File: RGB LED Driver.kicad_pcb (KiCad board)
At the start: 2 copper layers, 97.1 x 75.7 mm, 106 parts, among them J1 USB_C_Receptacle_USB2.0, J2 Conn_01x06_Pin, Q1 AO3400A, Q2 AO3400A, Q3 AO3400A, Q4 AO3400A, SW1 BOOT, U1 TPS61170DRVR, U10 LM358, U2 AP2112K-3.3TRG1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

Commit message: laid out stuff
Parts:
- removed kibuzzard-6592DDAB: G***, kibuzzard-6592DDAB
- added C16: 1uF, Capacitor_SMD:C_0805_2012Metric_Pad1.18x1.45mm_HandSolder, F.Cu at (90.0, 59.0)
- added C17: 1uF, Capacitor_SMD:C_0805_2012Metric_Pad1.18x1.45mm_HandSolder, F.Cu at (127.0, 83.7)
- added C18: 1uF, Capacitor_SMD:C_0805_2012Metric_Pad1.18x1.45mm_HandSolder, F.Cu at (127.0, 81.2)
- added D44: RED LED, LED_SMD:LED_0805_2012Metric_Pad1.15x1.40mm_HandSolder, F.Cu at (171.0, 86.5)
- added R28: 10K, Resistor_SMD:R_0805_2012Metric_Pad1.20x1.40mm_HandSolder, F.Cu at (109.5, 78.0)
- added R29: 300K, Resistor_SMD:R_0805_2012Metric_Pad1.20x1.40mm_HandSolder, F.Cu at (168.0, 86.5)
- added TP1: 5260 (Red), TestPoint:TestPoint_Keystone_5000-5004_Miniature, F.Cu at (143.5, 57.0)
- added TP2: 5264 (Yellow), TestPoint:TestPoint_Keystone_5000-5004_Miniature, F.Cu at (174.0, 86.0)
- added TP3: 5261 (Black), TestPoint:TestPoint_Keystone_5000-5004_Miniature, F.Cu at (143.5, 68.0)
- added TP4: 5261 (Black), TestPoint:TestPoint_Keystone_5000-5004_Miniature, F.Cu at (165.0, 86.0)
- added TP5: 5269 (Purple), TestPoint:TestPoint_Keystone_5000-5004_Miniature, F.Cu at (117.5, 56.8)
- added TP6: 5269 (Purple), TestPoint:TestPoint_Keystone_5000-5004_Miniature, F.Cu at (117.5, 60.2)
- added TP7: 5269 (Purple), TestPoint:TestPoint_Keystone_5000-5004_Miniature, F.Cu at (117.5, 63.8)
- added TP8: 5269 (Purple), TestPoint:TestPoint_Keystone_5000-5004_Miniature, F.Cu at (117.5, 67.2)
- added kibuzzard-65932266: G***, kibuzzard-65932266, F.Cu at (143.5, 54.6)
- added kibuzzard-65932378: G***, kibuzzard-65932378, F.Cu at (165.0, 88.8)
- added kibuzzard-65932378: G***, kibuzzard-65932378, F.Cu at (143.5, 70.8)
- added kibuzzard-6593238E: G***, kibuzzard-6593238E, F.Cu at (174.0, 88.8)
- added kibuzzard-659323CF: G***, kibuzzard-659323CF, F.Cu at (131.5, 88.0)
- added kibuzzard-65932434: G***, kibuzzard-65932434, F.Cu at (106.2, 86.2)
- added kibuzzard-65932443: G***, kibuzzard-65932443, F.Cu at (156.0, 81.0)
- added kibuzzard-65932491: G***, kibuzzard-65932491, F.Cu at (99.0, 86.5)
- added kibuzzard-659324E3: G***, kibuzzard-659324E3, F.Cu at (117.0, 81.8)
- added kibuzzard-65932565: G***, kibuzzard-65932565, F.Cu at (90.0, 86.8)
- added kibuzzard-659325DE: G***, kibuzzard-659325DE, F.Cu at (142.8, 130.8)
- added kibuzzard-65932806: G***, kibuzzard-65932806, F.Cu at (100.5, 130.8)
- added kibuzzard-65932B20: G***, kibuzzard-65932B20, F.Cu at (122.2, 56.8)
- added kibuzzard-65932B45: G***, kibuzzard-65932B45, F.Cu at (122.2, 67.2)
- added kibuzzard-65932B4E: G***, kibuzzard-65932B4E, F.Cu at (122.2, 63.8)
- added kibuzzard-65932B54: G***, kibuzzard-65932B54, F.Cu at (122.2, 60.2)
- added kibuzzard-65932F0E: G***, kibuzzard-65932F0E, F.Cu at (89.0, 125.0)
- added kibuzzard-65932F14: G***, kibuzzard-65932F14, F.Cu at (89.0, 115.0)
- added kibuzzard-65932F1A: G***, kibuzzard-65932F1A, F.Cu at (88.9, 105.4)
- added kibuzzard-65932F21: G***, kibuzzard-65932F21, F.Cu at (88.9, 95.2)
- added kibuzzard-6593379A: G***, kibuzzard-6593379A, F.Cu at (147.5, 84.5)
- C11: value 10uF -> 1uF
- C2: footprint rgb_led_driver_footprints:EEHZA1J100P -> Capacitor_SMD:CP_Elec_6.3x5.8
- J2: footprint Connector_PinSocket_2.54mm:PinSocket_1x06_P2.54mm_Vertical -> Connector_PinHeader_2.54mm:PinHeader_1x06_P2.54mm_Vertical
- moved R7 58.2 mm to (143.5, 60.0)
- moved D2 52.8 mm to (143.5, 63.5)
- moved NT1 30.6 mm to (169.4, 84.0)
- moved D3 19.0 mm to (90.0, 77.0)
- moved R14 17.0 mm to (90.0, 80.5), turned to 180 degrees
- moved C7 16.0 mm to (90.0, 65.0), turned to 0 degrees
- moved U5 15.4 mm to (133.6, 80.0), turned to -90 degrees
- moved J2 12.8 mm to (98.9, 83.0)
- moved C13 10.4 mm to (94.6, 105.2)
- moved C14 10.3 mm to (94.6, 115.0)
- moved C15 10.3 mm to (94.6, 124.8)
- moved C12 10.2 mm to (94.5, 95.1)
- moved R23 9.57 mm to (111.8, 127.2), turned to 0 degrees
- moved R8 9.44 mm to (111.8, 107.4), turned to 0 degrees
- moved R17 9.37 mm to (111.8, 97.3), turned to 0 degrees
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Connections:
- C10 pad 1: +3.3V -> +3V3
- C9 pad 1: +3.3V -> +3V3
- U4 pad 1: Net-(J1-D+-PadA6) -> /USB-Serial/USB_N
- U4 pad 3: Net-(J1-D--PadA7) -> /USB-Serial/USB_P
- U4 pad 4: /USB-Serial/USB_N -> Net-(J1-D+-PadA6)
- U4 pad 6: /USB-Serial/USB_P -> Net-(J1-D--PadA7)
- U5 pad 16: unconnected-(U5-VPP-Pad16) -> Net-(U5-VPP)
- U5 pad 5: +3.3V -> +3V3
- U5 pad 6: +3.3V -> +3V3
- U5 pad 7: +3.3V -> +5V
- U6 pad 27: /ESP32/LED_R -> unconnected-(U6-IO16-Pad27)
- U6 pad 28: /ESP32/LED_G -> /ESP32/LED_W
- U6 pad 30: /ESP32/LED_B -> unconnected-(U6-IO18-Pad30)
- U6 pad 31: /ESP32/LED_W -> /ESP32/LED_B
- U6 pad 33: unconnected-(U6-IO21-Pad33) -> /ESP32/LED_G
- U6 pad 36: unconnected-(U6-IO22-Pad36) -> /ESP32/LED_R
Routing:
- net +5V: track 58.3 -> 280.2 mm, vias 2 -> 5
- net /ESP32/LED_W: track 0.00 -> 82.3 mm, vias 0 -> 2
- net /ESP32/LED_B: track 0.00 -> 76.4 mm, vias 0 -> 2
- net /ESP32/DTR: track 0.00 -> 71.1 mm, vias 0 -> 1
- net /ESP32/LED_G: track 0.00 -> 69.8 mm, vias 0 -> 2
- net /ESP32/TX_CP2102_RX_ESP: track 0.47 -> 69.3 mm, vias 0 -> 1
- net /ESP32/RX_CP2102_TX_ESP: track 0.00 -> 68.6 mm
- net +36V: track 24.7 -> 89.2 mm
- net +3.3V: track 0.00 -> 54.3 mm, vias 0 -> 4
- net /ESP32/LED_R: track 0.00 -> 51.9 mm, vias 0 -> 2
- net /ESP32/RTS: track 0.00 -> 50.2 mm, vias 0 -> 2
- net Net-(NT1-Pad2): track 0.00 -> 43.6 mm
- net /ESP32/RESETn: track 0.00 -> 27.0 mm
- net /ESP32/GPIO0: track 0.00 -> 23.5 mm, vias 0 -> 2
- net GND: track 0.00 -> 15.8 mm, vias 0 -> 701
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- added copper zone on B.Cu, net GND
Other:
- board size 97.1 x 75.7 mm -> 97.5 x 79 mm
- board text added: "RGB LED Light Rev A DG/WS 1/24 MIT PCB Class | pcb.mit.edu github.com/PCB-Design-MIT/ Wi-Fi-Controlled-RGB-Light"

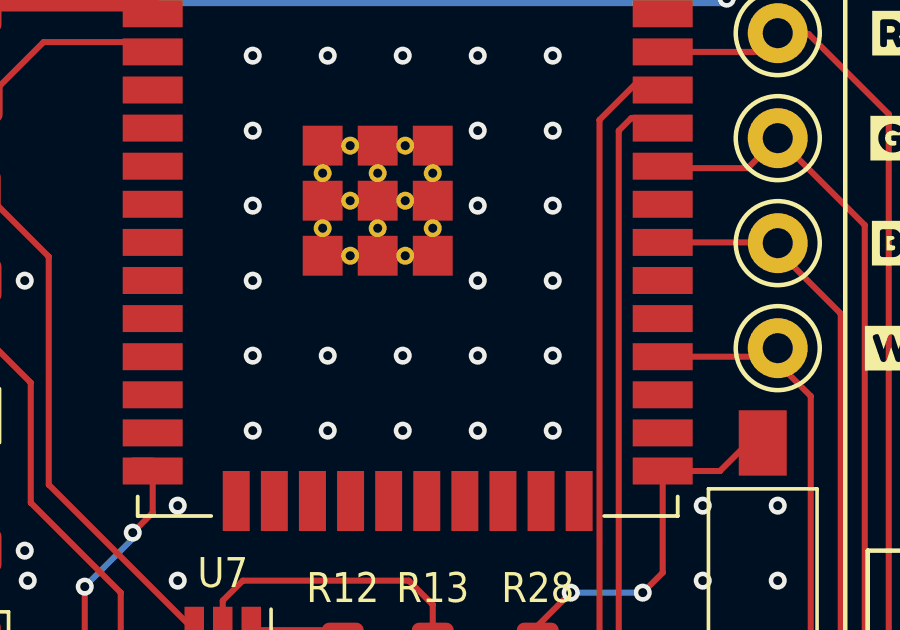
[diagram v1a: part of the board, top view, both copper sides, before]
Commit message: added silk for PCBWay to remove customer order
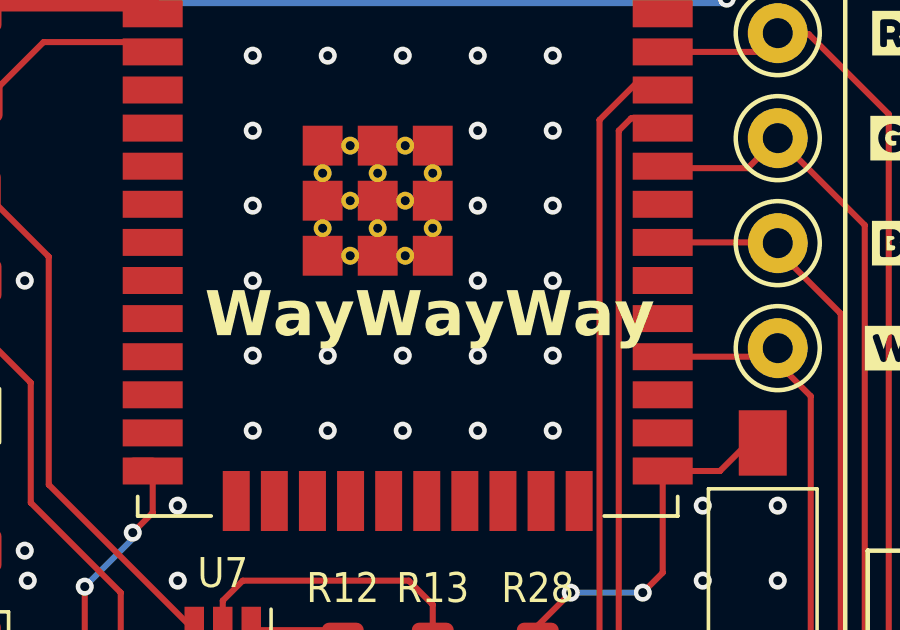
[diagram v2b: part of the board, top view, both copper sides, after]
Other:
- board text added: "WayWayWay"
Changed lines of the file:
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@@
     (attr board_only exclude_from_pos_files exclude_from_bom)
     (fp_text reference "kibuzzard-65932F0E" (at 0 -4.583106) (layer "F.SilkS") hide
-        (effects (font (size 0 0)))
+        (effects (font (size 0 0) (thickness 0.15)))
     )
     (fp_text value "G***" (at 0 4.583106) (layer "F.SilkS") hide
-        (effects (font (size 0 0)))
+        (effects (font (size 0 0) (thickness 0.15)))
     )
     (fp_poly
@@
     (attr board_only exclude_from_pos_files exclude_from_bom)
     (fp_text reference "kibuzzard-659323CF" (at 0 -4.004204) (layer "F.SilkS") hide
-        (effects (font (size 0 0.9)))
+        (effects (font (size 0 0.9) (thickness 0.15)))
     )
     (fp_text value "G***" (at 0 4.004204) (layer "F.SilkS") hide
-        (effects (font (size 0 0.9)))
+        (effects (font (size 0 0.9) (thickness 0.15)))
     )
     (fp_poly
@@
     (attr board_only exclude_from_pos_files exclude_from_bom)
     (fp_text reference "kibuzzard-65932F14" (at 0 -4.579931) (layer "F.SilkS") hide
-        (effects (font (size 0 0)))
+        (effects (font (size 0 0) (thickness 0.15)))
     )
     (fp_text value "G***" (at 0 4.579931) (layer "F.SilkS") hide
-        (effects (font (size 0 0)))
+        (effects (font (size 0 0) (thickness 0.15)))
     )
     (fp_poly
@@
     (attr board_only exclude_from_pos_files exclude_from_bom)
     (fp_text reference "kibuzzard-65932378" (at 0 -3.792643) (layer "F.SilkS") hide
-        (effects (font (size 0 0.9)))
+        (effects (font (size 0 0.9) (thickness 0.15)))
     )
     (fp_text value "G***" (at 0 3.792643) (layer "F.SilkS") hide
-        (effects (font (size 0 0.9)))
+        (effects (font (size 0 0.9) (thickness 0.15)))
     )
     (fp_poly
@@
     (attr board_only exclude_from_pos_files exclude_from_bom)
     (fp_text reference "kibuzzard-65932F1A" (at 0 -4.587551) (layer "F.SilkS") hide
-        (effects (font (size 0 0)))
+        (effects (font (size 0 0) (thickness 0.15)))
     )
     (fp_text value "G***" (at 0 4.587551) (layer "F.SilkS") hide
-        (effects (font (size 0 0)))
+        (effects (font (size 0 0) (thickness 0.15)))
     )
     (fp_poly
@@
     (attr board_only exclude_from_pos_files exclude_from_bom)
     (fp_text reference "kibuzzard-65932F21" (at 0 -4.579931) (layer "F.SilkS") hide
-        (effects (font (size 0 0)))
+        (effects (font (size 0 0) (thickness 0.15)))
     )
     (fp_text value "G***" (at 0 4.579931) (layer "F.SilkS") hide
-        (effects (font (size 0 0)))
+        (effects (font (size 0 0) (thickness 0.15)))
     )
     (fp_poly
@@
     (attr board_only exclude_from_pos_files exclude_from_bom)
     (fp_text reference "kibuzzard-65932266" (at 0 -3.790738) (layer "F.SilkS") hide
-        (effects (font (size 0 0.9)))
+        (effects (font (size 0 0.9) (thickness 0.15)))
     )
     (fp_text value "G***" (at 0 3.790738) (layer "F.SilkS") hide
-        (effects (font (size 0 0.9)))
+        (effects (font (size 0 0.9) (thickness 0.15)))
     )
     (fp_poly
@@
     (attr board_only exclude_from_pos_files exclude_from_bom)
     (fp_text reference "kibuzzard-659325DE" (at 0 -3.968485) (layer "F.SilkS") hide
-        (effects (font (size 0 0)))
+        (effects (font (size 0 0) (thickness 0.15)))
     )
     (fp_text value "G***" (at 0 3.968485) (layer "F.SilkS") hide
-        (effects (font (size 0 0)))
+        (effects (font (size 0 0) (thickness 0.15)))
     )
     (fp_poly
@@
     (attr board_only exclude_from_pos_files exclude_from_bom)
     (fp_text reference "kibuzzard-659324E3" (at 0 -3.791373) (layer "F.SilkS") hide
-        (effects (font (size 0 0)))
+        (effects (font (size 0 0) (thickness 0.15)))
     )
     (fp_text value "G***" (at 0 3.791373) (layer "F.SilkS") hide
-        (effects (font (size 0 0)))
+        (effects (font (size 0 0) (thickness 0.15)))
     )
     (fp_poly
@@
     (attr board_only exclude_from_pos_files exclude_from_bom)
     (fp_text reference "kibuzzard-6593379A" (at 0 -3.778673) (layer "F.SilkS") hide
-        (effects (font (size 0 0)))
+        (effects (font (size 0 0) (thickness 0.15)))
     )
     (fp_text value "G***" (at 0 3.778673) (layer "F.SilkS") hide
-        (effects (font (size 0 0)))
+        (effects (font (size 0 0) (thickness 0.15)))
     )
     (fp_poly
@@
     (attr board_only exclude_from_pos_files exclude_from_bom)
     (fp_text reference "kibuzzard-65932B54" (at 0 -3.792643) (layer "F.SilkS") hide
-        (effects (font (size 0 0)))
+        (effects (font (size 0 0) (thickness 0.15)))
     )
     (fp_text value "G***" (at 0 3.792643) (layer "F.SilkS") hide
-        (effects (font (size 0 0)))
+        (effects (font (size 0 0) (thickness 0.15)))
     )
     (fp_poly
@@
     (attr board_only exclude_from_pos_files exclude_from_bom)
     (fp_text reference "kibuzzard-65932443" (at 0 -4.043892) (layer "F.SilkS") hide
-        (effects (font (size 0 0.9)))
+        (effects (font (size 0 0.9) (thickness 0.15)))
     )
     (fp_text value "G***" (at 0 4.043892) (layer "F.SilkS") hide
-        (effects (font (size 0 0.9)))
+        (effects (font (size 0 0.9) (thickness 0.15)))
     )
     (fp_poly
@@
     (attr board_only exclude_from_pos_files exclude_from_bom)
     (fp_text reference "kibuzzard-65932B4E" (at 0 -3.792643) (layer "F.SilkS") hide
-        (effects (font (size 0 0)))
+        (effects (font (size 0 0) (thickness 0.15)))
     )
     (fp_text value "G***" (at 0 3.792643) (layer "F.SilkS") hide
-        (effects (font (size 0 0)))
+        (effects (font (size 0 0) (thickness 0.15)))
     )
     (fp_poly
@@
     (attr board_only exclude_from_pos_files exclude_from_bom)
     (fp_text reference "kibuzzard-65932491" (at 0 -3.792643 -90) (layer "F.SilkS") hide
-        (effects (font (size 0 0.9)))
+        (effects (font (size 0 0.9) (thickness 0.15)))
     )
     (fp_text value "G***" (at 0 3.792643 -90) (layer "F.SilkS") hide
-        (effects (font (size 0 0.9)))
+        (effects (font (size 0 0.9) (thickness 0.15)))
     )
     (fp_poly
@@
     (attr board_only exclude_from_pos_files exclude_from_bom)
     (fp_text reference "kibuzzard-65932434" (at 0 -3.961342) (layer "F.SilkS") hide
-        (effects (font (size 0 0.9)))
+        (effects (font (size 0 0.9) (thickness 0.15)))
     )
     (fp_text value "G***" (at 0 3.961342) (layer "F.SilkS") hide
-        (effects (font (size 0 0.9)))
+        (effects (font (size 0 0.9) (thickness 0.15)))
     )
     (fp_poly
@@
     (attr board_only exclude_from_pos_files exclude_from_bom)
     (fp_text reference "kibuzzard-65932806" (at 0 -4.002617) (layer "F.SilkS") hide
-        (effects (font (size 0 0)))
+        (effects (font (size 0 0) (thickness 0.15)))
     )
     (fp_text value "G***" (at 0 4.002617) (layer "F.SilkS") hide
-        (effects (font (size 0 0)))
+        (effects (font (size 0 0) (thickness 0.15)))
     )
     (fp_poly
@@
     (attr board_only exclude_from_pos_files exclude_from_bom)
     (fp_text reference "kibuzzard-65932B20" (at 0 -3.792643) (layer "F.SilkS") hide
-        (effects (font (size 0 0)))
+        (effects (font (size 0 0) (thickness 0.15)))
     )
     (fp_text value "G***" (at 0 3.792643) (layer "F.SilkS") hide
-        (effects (font (size 0 0)))
+        (effects (font (size 0 0) (thickness 0.15)))
     )
     (fp_poly
@@
     (attr board_only exclude_from_pos_files exclude_from_bom)
     (fp_text reference "kibuzzard-65932B45" (at 0 -3.792643) (layer "F.SilkS") hide
-        (effects (font (size 0 0)))
+        (effects (font (size 0 0) (thickness 0.15)))
     )
     (fp_text value "G***" (at 0 3.792643) (layer "F.SilkS") hide
-        (effects (font (size 0 0)))
+        (effects (font (size 0 0) (thickness 0.15)))
     )
     (fp_poly
@@
     (attr board_only exclude_from_pos_files exclude_from_bom)
     (fp_text reference "kibuzzard-6593238E" (at 0 -3.793278) (layer "F.SilkS") hide
-        (effects (font (size 0 0.9)))
+        (effects (font (size 0 0.9) (thickness 0.15)))
     )
     (fp_text value "G***" (at 0 3.793278) (layer "F.SilkS") hide
-        (effects (font (size 0 0.9)))
+        (effects (font (size 0 0.9) (thickness 0.15)))
     )
     (fp_poly
@@
     (attr board_only exclude_from_pos_files exclude_from_bom)
     (fp_text reference "kibuzzard-65932565" (at 0 -4.912783) (layer "F.SilkS") hide
-        (effects (font (size 0 0)))
+        (effects (font (size 0 0) (thickness 0.15)))
     )
     (fp_text value "G***" (at 0 4.912783) (layer "F.SilkS") hide
-        (effects (font (size 0 0)))
+        (effects (font (size 0 0) (thickness 0.15)))
     )
     (fp_poly
@@
     (effects (font (size 2 2) (thickness 0.5) bold) (justify mirror))
   )
+  (gr_text "WayWayWay" (at 98.4 67) (layer "F.SilkS")
+    (effects (font (size 1.5 1.5) (thickness 0.3) bold) (justify left bottom))
+  )
   (segment (start 148.25 65.4) (end 150.8125 67.9625) (width 0.25) (layer "F.Cu") (net 1))

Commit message: updated pcb with BOM
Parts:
- C17: value 1uF -> 4.7uF
- C2: value 10uF -> 10uF/63V
- C9: value 100nf -> 100nF
- D1: value SS35 -> SS36
- D3: value LED -> RED LED
- J1: value USB_C_Receptacle_USB2.0 -> USB4085
- NT1: value NetTie_2 -> Nettie
- R10, R16, R19, R22: value 5.1K -> 51K
- R14: value 1K -> 2K
- R17, R20, R23, R8: value 22R -> 100R
- R4: value 10.5K -> 10K/1%
- moved TP1 0.14 mm to (143.6, 56.9)
- moved R7 0.10 mm to (143.4, 60.0)
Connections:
- net /ESP32/LED_B renamed /BSig
- net /ESP32/LED_G renamed /GSig
- net /ESP32/LED_R renamed /RSig
- net /ESP32/LED_W renamed /WSig
- net Net-(J1-D+-PadA6) renamed /USB_C/USB_IN_P
- net Net-(J1-D--PadA7) renamed /USB_C/USB_IN_N
- net Net-(Q1-S) renamed /LED Driver G/Ifb
- net Net-(Q2-S) renamed /LED Driver R/Ifb
- net Net-(Q3-S) renamed /LED Driver B/Ifb
- net Net-(Q4-S) renamed /LED Driver W/Ifb
- net Net-(U10A-+) renamed /LED Driver W/VSet_2V0
- net Net-(U3A-+) renamed /LED Driver G/VSet_2V0
- net Net-(U8A-+) renamed /LED Driver R/VSet_2V0
- net Net-(U9A-+) renamed /LED Driver B/VSet_2V0
